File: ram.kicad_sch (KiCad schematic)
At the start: 1 part, among them IC5 MT41K256M16TW-107_P

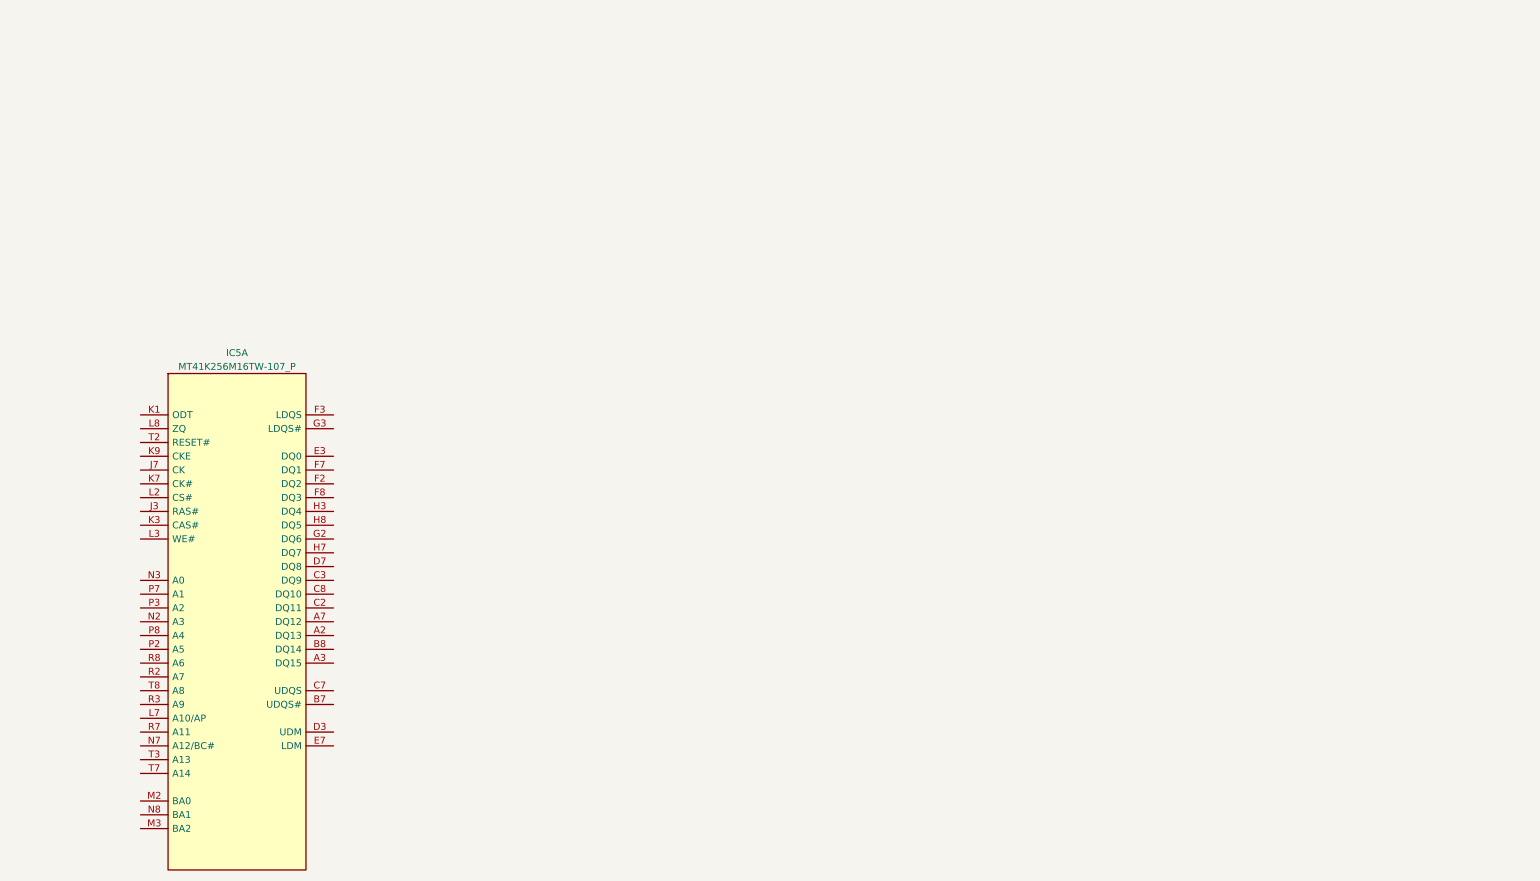
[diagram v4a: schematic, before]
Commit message: Add Labels for DDR & DDR Power
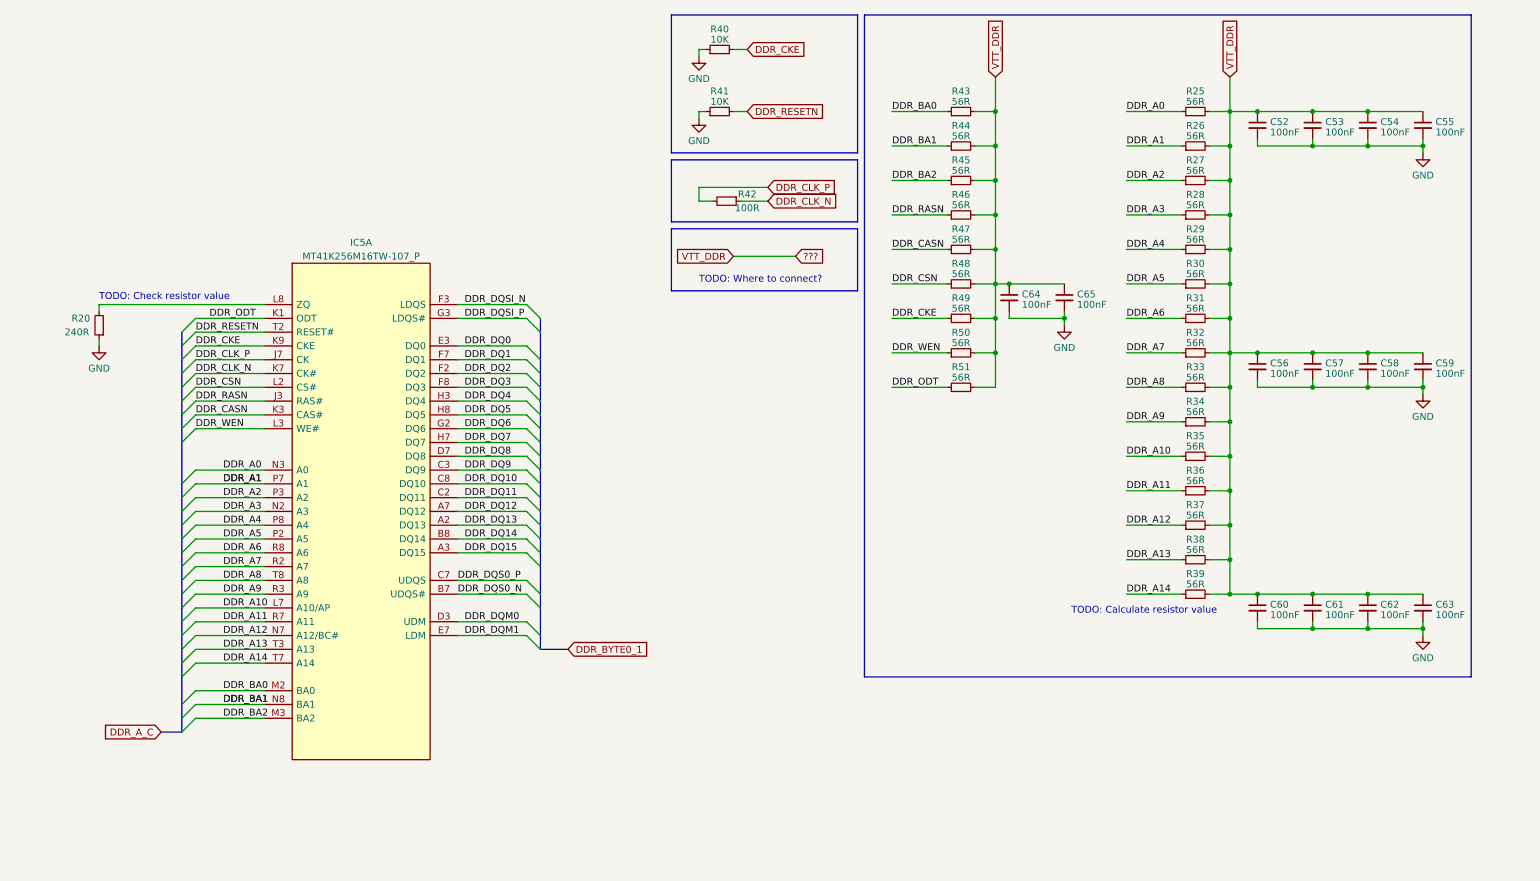
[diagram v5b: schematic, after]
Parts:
- added C52, C53, C54, C55, C56, C57, C58, C59, C60, C61, C62, C63, C64, C65: 100nF, symbol Device:C_Small
- added R20: 240R, symbol Device:R_Small
- added R25, R26, R27, R28, R29, R30, R31, R32, R33, R34, R35, R36, R37, R38, R39, R43, R44, R45, R46, R47, R48, R49, R50, R51: 56R, symbol Device:R_Small
- added R40, R41: 10K, symbol Device:R_Small
- added R42: 100R, symbol Device:R_Small
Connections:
- net DDR_DQ13: now reaches IC5.A2 (DQ13)
- net DDR_DQ15: now reaches IC5.A3 (DQ15)
- net DDR_DQ12: now reaches IC5.A7 (DQ12)
- net DDR_DQS0_N: now reaches IC5.B7 (UDQS#)
- net DDR_DQ14: now reaches IC5.B8 (DQ14)
- net DDR_DQ11: now reaches IC5.C2 (DQ11)
- net DDR_DQ9: now reaches IC5.C3 (DQ9)
- net DDR_DQS0_P: now reaches IC5.C7 (UDQS)
- net DDR_DQ10: now reaches IC5.C8 (DQ10)
- net DDR_DQM0: now reaches IC5.D3 (UDM)
- net DDR_DQ8: now reaches IC5.D7 (DQ8)
- net DDR_DQ0: now reaches IC5.E3 (DQ0)
- net DDR_DQM1: now reaches IC5.E7 (LDM)
- net DDR_DQ2: now reaches IC5.F2 (DQ2)
- net DDR_DQSI_N: now reaches IC5.F3 (LDQS)
- net DDR_DQ1: now reaches IC5.F7 (DQ1)
- net DDR_DQ3: now reaches IC5.F8 (DQ3)
- net DDR_DQ6: now reaches IC5.G2 (DQ6)
- net DDR_DQSI_P: now reaches IC5.G3 (LDQS#)
- net DDR_DQ4: now reaches IC5.H3 (DQ4)
- net DDR_DQ7: now reaches IC5.H7 (DQ7)
- net DDR_DQ5: now reaches IC5.H8 (DQ5)
- net DDR_RASN: now reaches IC5.J3 (RAS#)
- net DDR_RASN: now also R46.1
- net DDR_CLK_P: now reaches IC5.J7 (CK)
- net DDR_CLK_P: now also R42.2
- net DDR_ODT: now reaches IC5.K1 (ODT)
- net DDR_ODT: now also R51.1
- net DDR_CASN: now reaches IC5.K3 (CAS#)
- net DDR_CASN: now also R47.1
- net DDR_CLK_N: now reaches IC5.K7 (CK#)
- net DDR_CLK_N: now also R42.1
- net DDR_CKE: now reaches IC5.K9 (CKE)
- net DDR_CKE: now also R40.2, R49.1
- net DDR_CSN: now reaches IC5.L2 (CS#)
- net DDR_CSN: now also R48.1
- net DDR_WEN: now reaches IC5.L3 (WE#)
- net DDR_WEN: now also R50.1
- net DDR_A10: now reaches IC5.L7 (A10/AP)
- net DDR_A10: now also R35.1
- net at IC5.L8 (ZQ): now also R20.2
- net DDR_BA0: now reaches IC5.M2 (BA0)
- net DDR_BA0: now also R43.1
- net DDR_BA2: now reaches IC5.M3 (BA2)
- net DDR_BA2: now also R45.1
- net DDR_A3: now reaches IC5.N2 (A3)
- net DDR_A3: now also R28.1
- net DDR_A0: now reaches IC5.N3 (A0)
- net DDR_A0: now also R25.1
- net DDR_A12: now reaches IC5.N7 (A12/BC#)
- net DDR_A12: now also R37.1
- net DDR_BA1: now reaches IC5.N8 (BA1)
- net DDR_BA1: now also R44.1
- net DDR_A5: now reaches IC5.P2 (A5)
- net DDR_A5: now also R30.1
- net DDR_A2: now reaches IC5.P3 (A2)
- net DDR_A2: now also R27.1
- net DDR_A1: now reaches IC5.P7 (A1)
- net DDR_A1: now also R26.1
- net DDR_A4: now reaches IC5.P8 (A4)
- net DDR_A4: now also R29.1
- net DDR_A7: now reaches IC5.R2 (A7)
- net DDR_A7: now also R32.1
- net DDR_A9: now reaches IC5.R3 (A9)
- net DDR_A9: now also R34.1
- net DDR_A11: now reaches IC5.R7 (A11)
- net DDR_A11: now also R36.1
- net DDR_A6: now reaches IC5.R8 (A6)
- net DDR_A6: now also R31.1
- net DDR_RESETN: now reaches IC5.T2 (RESET#)
- net DDR_RESETN: now also R41.2
- net DDR_A13: now reaches IC5.T3 (A13)
- net DDR_A13: now also R38.1
- net DDR_A14: now reaches IC5.T7 (A14)
- net DDR_A14: now also R39.1
- net DDR_A8: now reaches IC5.T8 (A8)
- net DDR_A8: now also R33.1
- new net ???: C52.1, C53.1, C54.1, C55.1, C56.1, C57.1, C58.1, C59.1, C60.1, C61.1, C62.1, C63.1, C64.1, C65.1, R25.2, R26.2, R27.2, R28.2, R29.2, R30.2, R31.2, R32.2, R33.2, R34.2, R35.2, R36.2, R37.2, R38.2, R39.2, R43.2, R44.2, R45.2, R46.2, R47.2, R48.2, R49.2, R50.2, R51.2
- new net GND: C52.2, C53.2, C54.2, C55.2, C56.2, C57.2, C58.2, C59.2, C60.2, C61.2, C62.2, C63.2, C64.2, C65.2, R20.1, R40.1, R41.1
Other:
- note added: "TODO: Calculate resistor value"
- note added: "TODO: Check resistor value"
- note added: "TODO: Where to connect?"
- moved on the sheet: IC5A

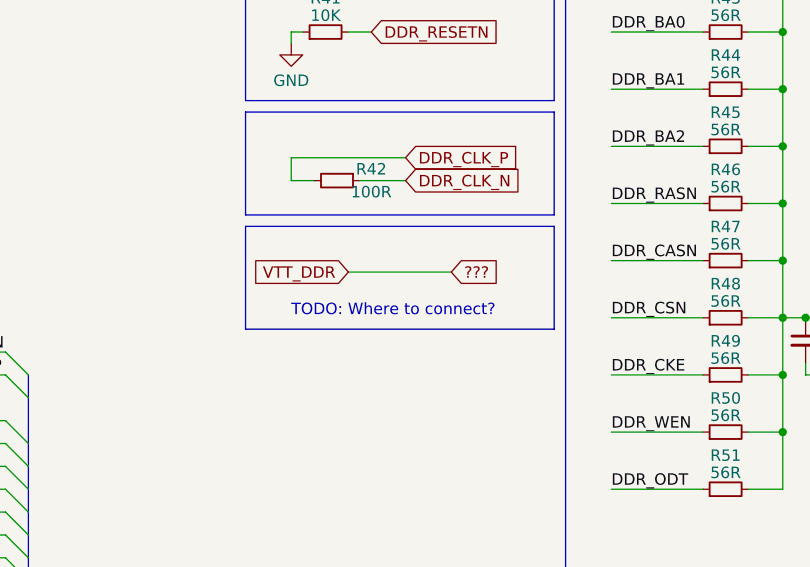
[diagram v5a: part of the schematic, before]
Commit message: Add DDR routing to STM32MP1
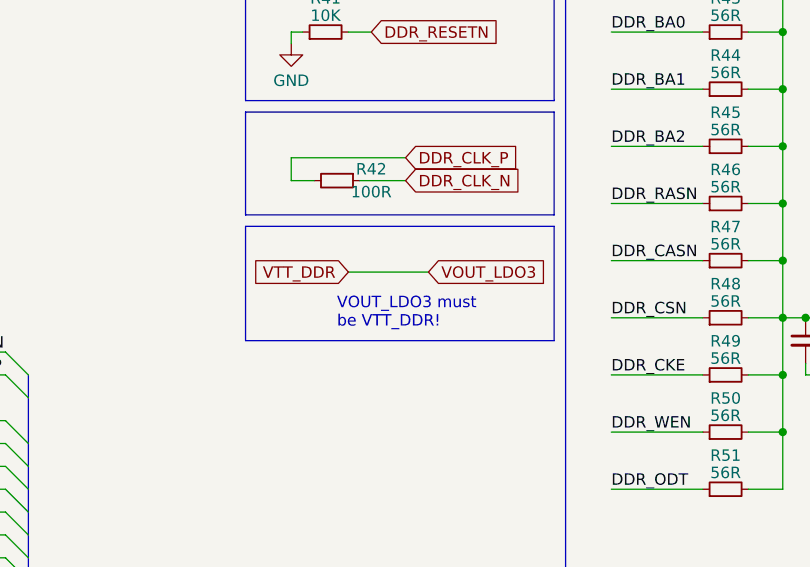
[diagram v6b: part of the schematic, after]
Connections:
- net ??? renamed VOUT_LDO3
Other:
- note added: "VOUT_LDO3 must be VTT_DDR!"
- note removed: "TODO: Where to connect?"
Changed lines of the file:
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@@
     (stroke (width 0) (type default))
   )
-  (wire (pts (xy 147.32 57.15) (xy 158.75 57.15))
+  (wire (pts (xy 147.32 57.15) (xy 156.21 57.15))
     (stroke (width 0) (type default))
   )
@@
     (fill (type none))
   )
-  (rectangle (start 135.89 52.07) (end 170.18 63.5)
+  (rectangle (start 135.89 52.07) (end 170.18 64.77)
     (stroke (width 0) (type default))
     (fill (type none))
@@
     (fill (type none))
   )
-  (text "TODO: Where to connect?" (at 140.97 62.23 0)
+  (text "VOUT_LDO3 must\nbe VTT_DDR!" (at 146.05 63.5 0)
     (effects (font (size 1.27 1.27)) (justify left bottom))
   )
@@
   (global_label "DDR_CLK_P" (shape input) (at 153.67 44.45 0) (fields_autoplaced)
     (effects (font (size 1.27 1.27)) (justify left))
+    (property "Intersheetrefs" "${INTERSHEET_REFS}" (at 0 0 0)
+      (effects (font (size 1.27 1.27)) hide)
+    )
   )
   (global_label "VTT_DDR" (shape input) (at 238.76 24.13 90) (fields_autoplaced)
@@
     )
   )
-  (global_label "???" (shape input) (at 158.75 57.15 0) (fields_autoplaced)
-    (effects (font (size 1.27 1.27)) (justify left))
-    (property "Intersheetrefs" "${INTERSHEET_REFS}" (at 164.9216 57.15 0)
-      (effects (font (size 1.27 1.27)) (justify left) hide)
-    )
-  )
   (global_label "DDR_RESETN" (shape input) (at 149.86 30.48 0) (fields_autoplaced)
     (effects (font (size 1.27 1.27)) (justify left))
@@
     )
   )
+  (global_label "VOUT_LDO3" (shape input) (at 156.21 57.15 0) (fields_autoplaced)
+    (effects (font (size 1.27 1.27)) (justify left))
+    (property "Intersheetrefs" "${INTERSHEET_REFS}" (at 169.6387 57.15 0)
+      (effects (font (size 1.27 1.27)) (justify left) hide)
+    )
+  )
   (global_label "DDR_CKE" (shape input) (at 149.86 19.05 0) (fields_autoplaced)
     (effects (font (size 1.27 1.27)) (justify left))
+    (property "Intersheetrefs" "${INTERSHEET_REFS}" (at 0 0 0)
+      (effects (font (size 1.27 1.27)) hide)
+    )
   )
   (global_label "DDR_BYTE0_1" (shape input) (at 116.84 129.54 0) (fields_autoplaced)
@@
   (global_label "DDR_CLK_N" (shape input) (at 153.67 46.99 0) (fields_autoplaced)
     (effects (font (size 1.27 1.27)) (justify left))
+    (property "Intersheetrefs" "${INTERSHEET_REFS}" (at 0 0 0)
+      (effects (font (size 1.27 1.27)) hide)
+    )
   )
   (global_label "VTT_DDR" (shape input) (at 195.58 24.13 90) (fields_autoplaced)

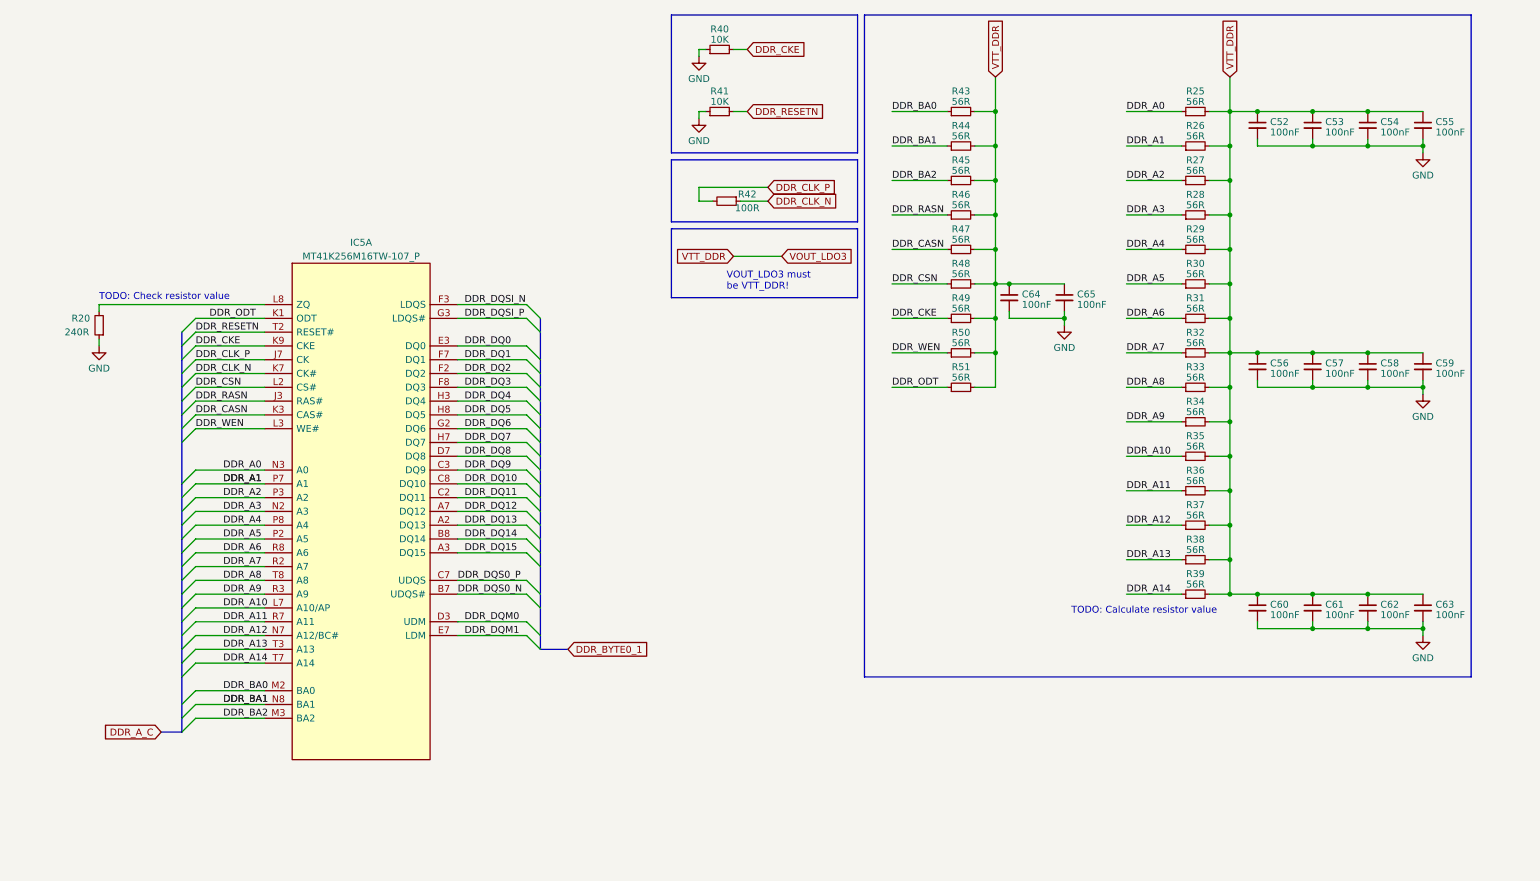
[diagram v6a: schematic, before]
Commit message: Add documentation to DDR routing
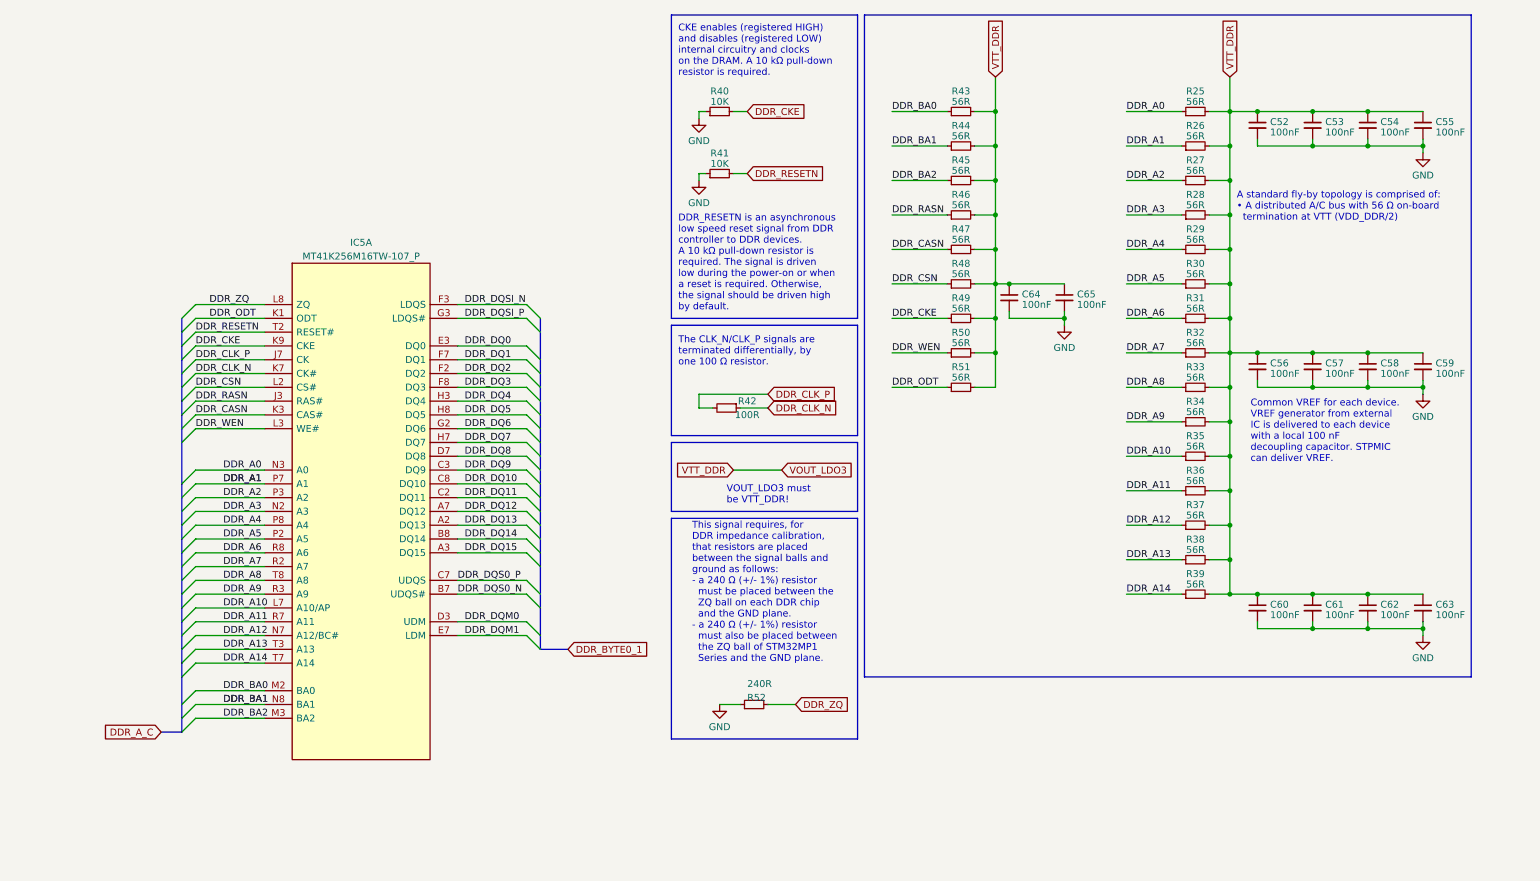
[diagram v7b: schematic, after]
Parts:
- removed R20: 240R, symbol Device:R_Small
- added R52: 240R, symbol Device:R_Small
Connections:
- net GND: now also R52.1
- net DDR_ZQ: now reaches IC5.L8 (ZQ)
- net DDR_ZQ: now also R52.2
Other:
- note added: "A standard fly-by topology is comprised of: • A distributed A/C bus with 56 Ω on-board termination at VTT (VDD_DDR/2)"
- note added: "CKE enables (registered HIGH) and disables (registered LOW) internal circuitry and clocks on the DRAM. A 10 kΩ pull-down resistor is required."
- note added: "Common VREF for each device. VREF generator from external IC is delivered to each device with a local 100 nF decoupling capacitor. STPMIC can deliver VREF."
- note added: "DDR_RESETN is an asynchronous low speed reset signal from DDR controller to DDR devices. A 10 kΩ pull-down resistor is required. The signal is driven low during the power-on or when a reset is required. Otherwise, the signal should be driven high by default."
- note added: "The CLK_N/CLK_P signals are terminated differentially, by one 100 Ω resistor."
- note added: "This signal requires, for DDR impedance calibration, that resistors are placed between the signal balls and ground as follows: - a 240 Ω (+/- 1%) resistor must be placed between the ZQ ball on each DDR chip and the GND plane. - a 240 Ω (+/- 1%) resistor must also be placed between the ZQ ball of STM32MP1 Series and the GND plane."
- note removed: "TODO: Calculate resistor value"
- note removed: "TODO: Check resistor value"
- moved on the sheet: R40, R41, R42
